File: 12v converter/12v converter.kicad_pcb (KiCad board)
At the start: 2 copper layers, 61.3 x 46 mm, 19 parts, among them J1 Conn_01x02_Socket, J2 Conn_01x02_Socket, U1 LM2674N-3.3

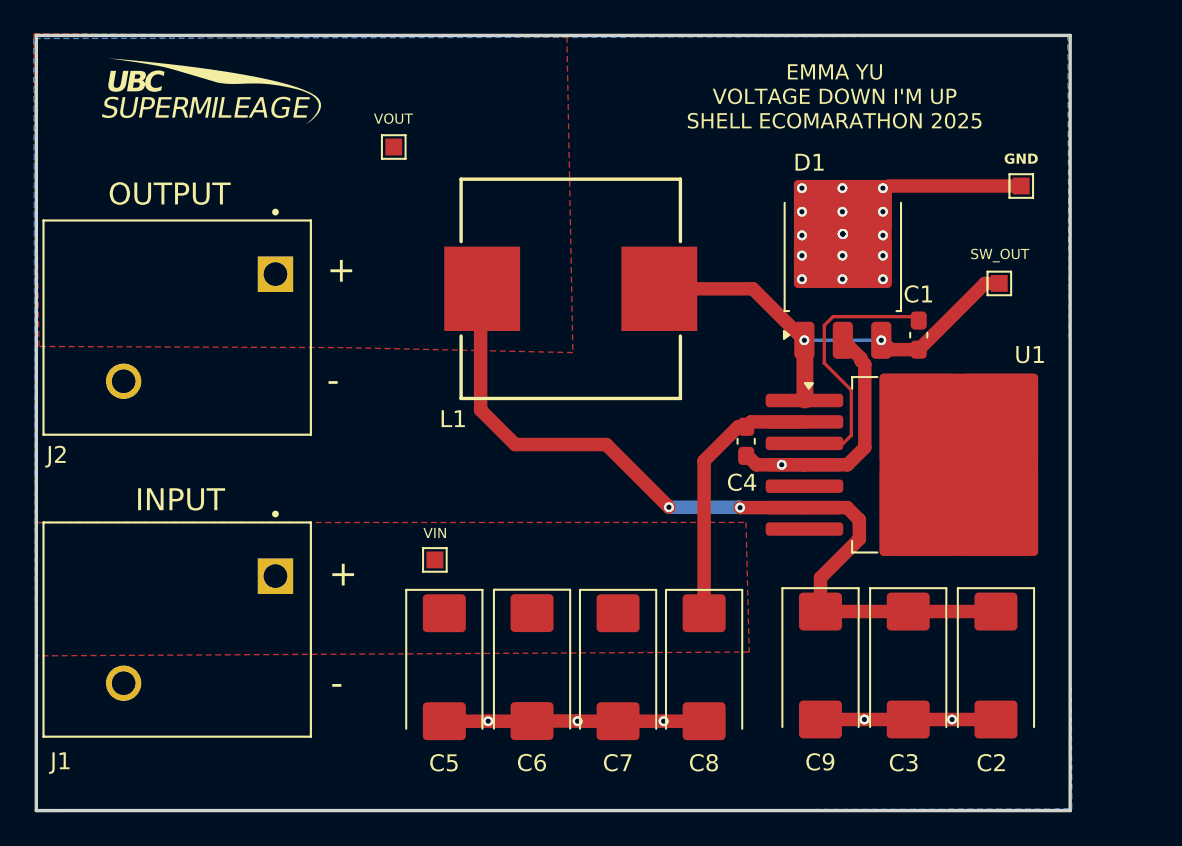
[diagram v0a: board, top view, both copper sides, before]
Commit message: Fixed silkscreen RefDes labels, made component values visible, added mounting holes with keepout zones around them. Generated gerber, drill and drill map files
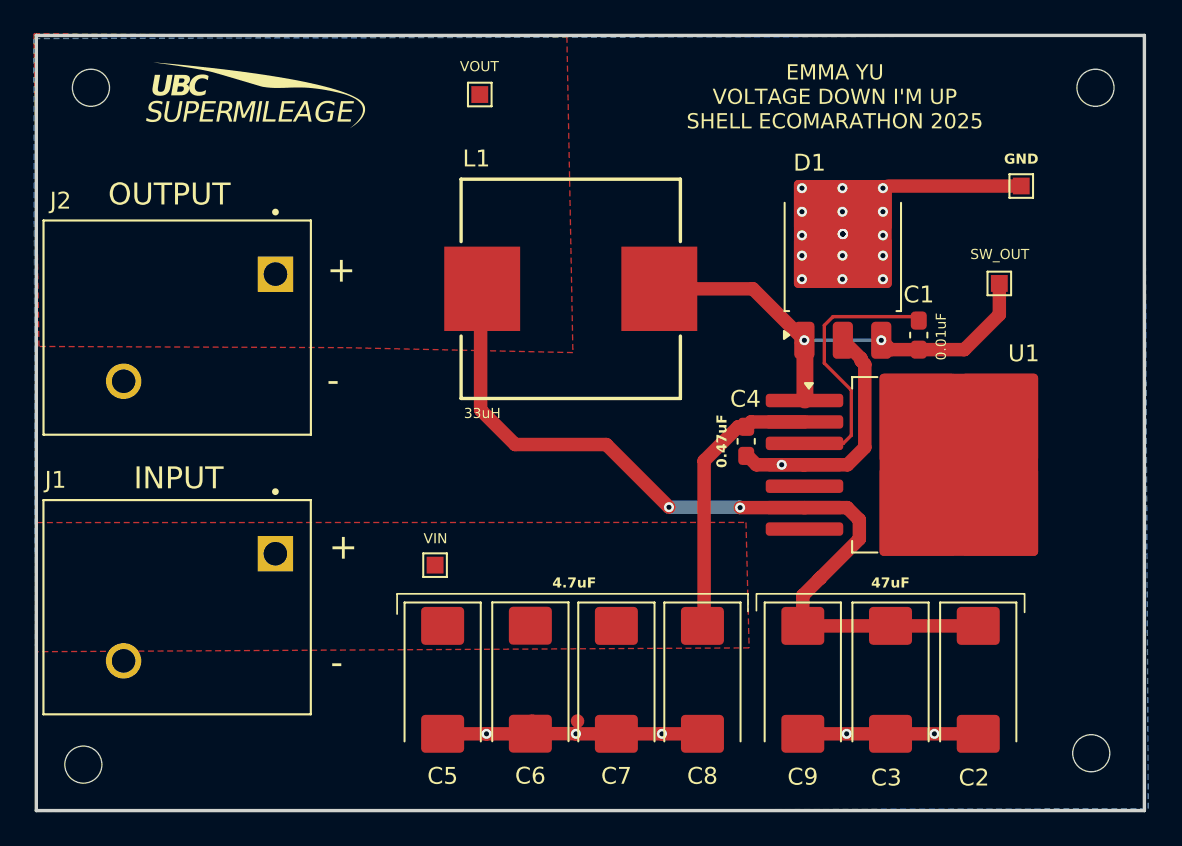
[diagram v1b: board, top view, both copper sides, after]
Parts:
- added H1: MountingHole, MountingHole:MountingHole_2.2mm_M2, F.Cu at (121.8, 88.8)
- added H2: MountingHole, MountingHole:MountingHole_2.2mm_M2, F.Cu at (181.4, 88.8)
- added H3: MountingHole, MountingHole:MountingHole_2.2mm_M2, F.Cu at (181.2, 128.3)
- added H4: MountingHole, MountingHole:MountingHole_2.2mm_M2, F.Cu at (121.4, 129.0)
- C1: value 0.01 uF -> 0.01uF
- C4: value 0.47 uF -> 0.47uF
- L1: value 33 uH -> 33uH
- moved VOUT 5.97 mm to (144.9, 89.2)
- moved G*** 2.63 mm to (131.6, 89.3)
- moved C2 1.35 mm to (174.4, 124.0)
- moved C3 1.35 mm to (169.2, 124.0)
- moved C9 1.35 mm to (164.1, 124.0)
- moved J1 1.33 mm to (119.0, 113.3)
- moved C5 0.76 mm to (142.7, 124.0)
- moved C6 0.76 mm to (147.9, 123.9)
- moved C7 0.76 mm to (153.0, 124.0)
- moved C8 0.76 mm to (158.1, 124.0)
- moved VIN 0.31 mm to (142.2, 117.2)
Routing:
- net /VOUT: track 50.6 -> 52.0 mm
- net /SW_OUT: track 27.1 -> 28.2 mm
- net VIN: track 15.9 -> 16.7 mm
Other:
- board size 61.3 x 46 mm -> 65.7 x 46 mm
- board text added: "4.7uF"
- board text added: "47uF"
